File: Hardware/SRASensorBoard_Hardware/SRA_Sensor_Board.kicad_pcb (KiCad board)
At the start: 2 copper layers, 124.5 x 92.7 mm, 106 parts, among them J1 USB_A, Q1 BSS138, Q10 BSS138, Q11 BSS138, Q12 BSS138, Q13 BSS138, Q2 BSS138, Q3 BSS138, Q4 BSS138, Q5 BSS138, Q6 BSS138, Q7 Q_PMOS_GDS, Q8 Q_NMOS_GSD, Q9 BSS138, U1 OKI, U2 OKI, U3 FT230XS, U4 TM4C129E_Launchpad

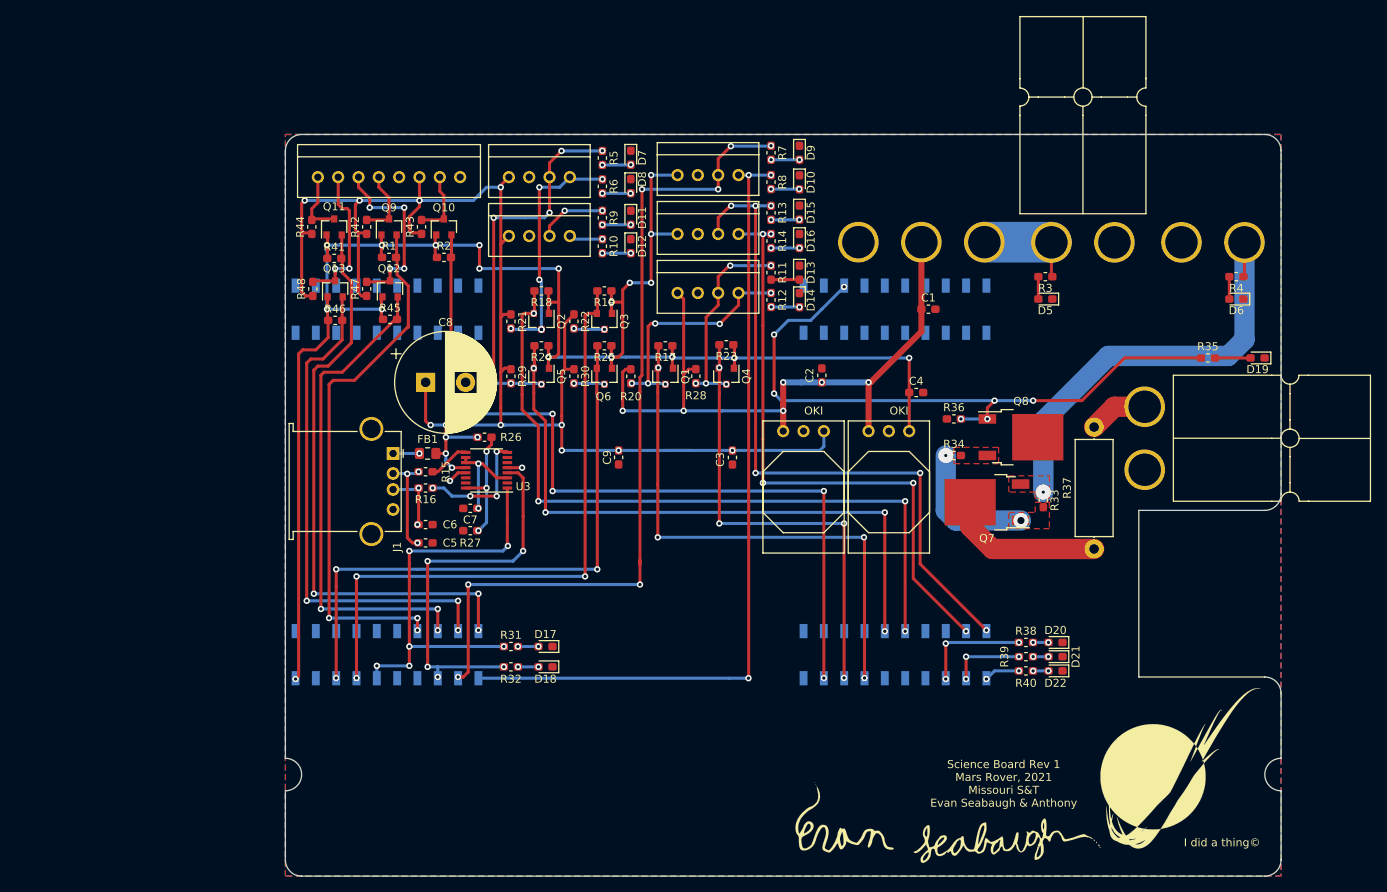
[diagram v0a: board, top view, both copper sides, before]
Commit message: Board Progress 6 (Post Review)
Finished moving vias off pads and labeling most things and added leds for spectrometer
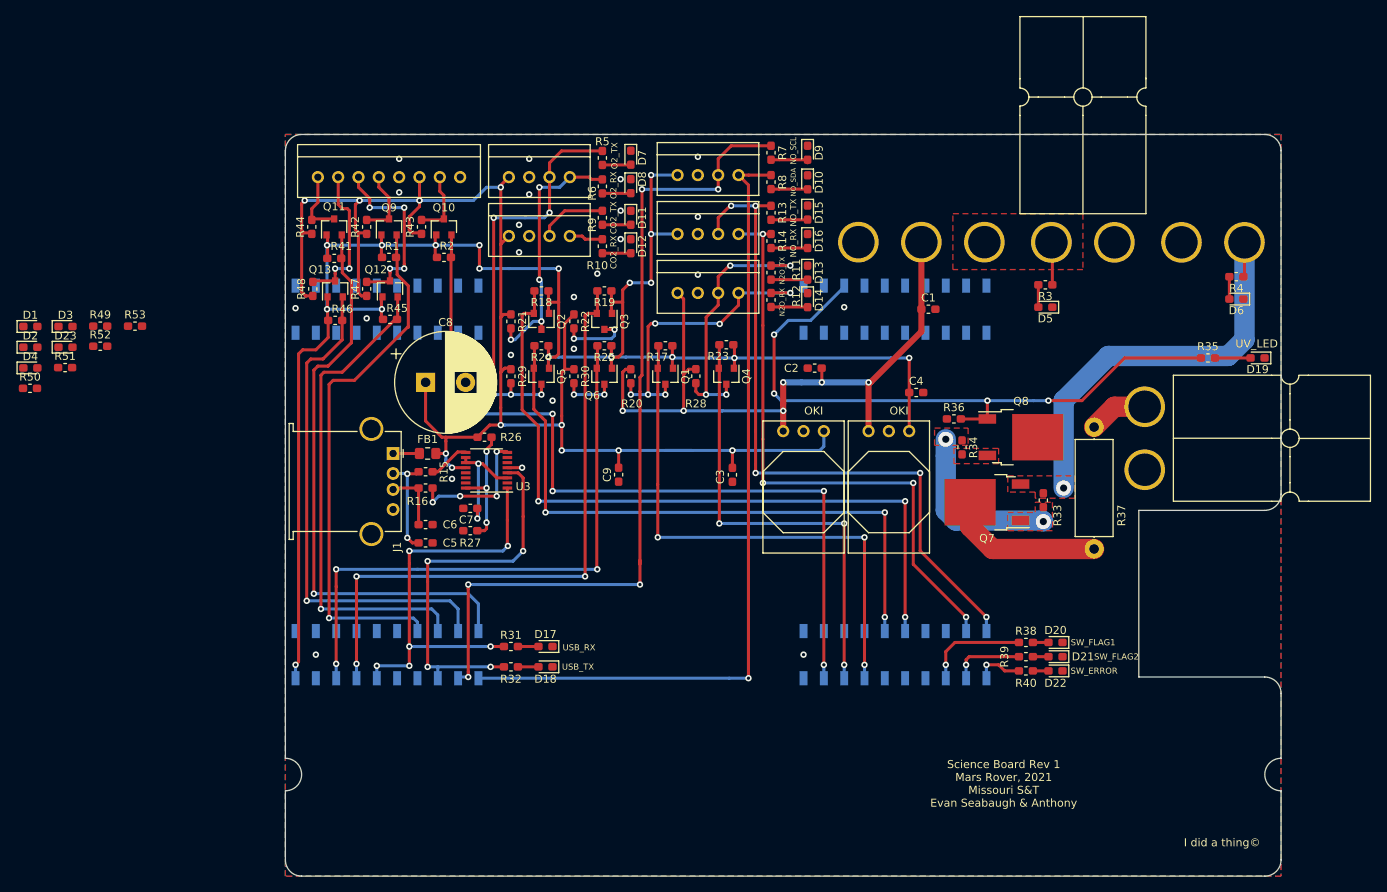
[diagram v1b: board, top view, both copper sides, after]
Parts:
- removed G***: LOGO, MRDT_Silkscreens:z_sig_Evan_Seabaugh_44mmx13.5mm
- removed G***: MRDT, MRDT_Silkscreens:0_MRDT_Logo_20mm
- added D1: LED, Diode_SMD:D_0603_1608Metric_Pad1.05x0.95mm_HandSolder, F.Cu at (59.6, 83.7)
- added D2: LED, Diode_SMD:D_0603_1608Metric_Pad1.05x0.95mm_HandSolder, F.Cu at (59.6, 86.3)
- added D23: LED, Diode_SMD:D_0603_1608Metric_Pad1.05x0.95mm_HandSolder, F.Cu at (64.0, 86.3)
- added D3: LED, Diode_SMD:D_0603_1608Metric_Pad1.05x0.95mm_HandSolder, F.Cu at (64.0, 83.7)
- added D4: LED, Diode_SMD:D_0603_1608Metric_Pad1.05x0.95mm_HandSolder, F.Cu at (59.6, 88.9)
- added R49: 330, Resistor_SMD:R_0603_1608Metric_Pad1.05x0.95mm_HandSolder, F.Cu at (68.3, 83.7)
- added R50: 330, Resistor_SMD:R_0603_1608Metric_Pad1.05x0.95mm_HandSolder, F.Cu at (59.5, 91.4)
- added R51: 330, Resistor_SMD:R_0603_1608Metric_Pad1.05x0.95mm_HandSolder, F.Cu at (63.9, 88.8)
- added R52: 330, Resistor_SMD:R_0603_1608Metric_Pad1.05x0.95mm_HandSolder, F.Cu at (68.3, 86.2)
- added R53: 330, Resistor_SMD:R_0603_1608Metric_Pad1.05x0.95mm_HandSolder, F.Cu at (72.6, 83.7)
- moved C3 2.16 mm to (147.3, 102.2)
- moved C9 2.16 mm to (133.1, 102.2)
- moved R34 1.44 mm to (176.0, 98.8), turned to 270 degrees
- moved C2 1.27 mm to (157.6, 88.9), turned to 180 degrees
- moved D5 1.02 mm to (186.4, 81.3)
- moved R3 1.02 mm to (186.4, 78.5)
- moved D10 1.02 mm to (156.7, 65.7)
- moved D13 1.02 mm to (156.7, 77.0)
- moved D14 1.02 mm to (156.7, 80.4)
- moved D15 1.02 mm to (156.7, 69.5)
- moved D16 1.02 mm to (156.7, 73.0)
- moved D9 1.02 mm to (156.7, 62.0)
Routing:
- net N2O_RX: track 29.9 -> 38.5 mm
- net N2O_TX: track 25.3 -> 33.7 mm, vias 5 -> 4
- net +12VA: track 12.7 -> 5.55 mm
- net Net-(Q7-Pad1): track 16.8 -> 21.7 mm
- net C02_RX: track 4.03 -> 8.74 mm
- net O2_TX: track 47.6 -> 51.5 mm, vias 7 -> 5
- net O2_RX: track 30.4 -> 33.0 mm, vias 6 -> 4
- net Net-(C7-Pad1): track 12.2 -> 14.8 mm
- net C02_TX: track 4.03 -> 6.51 mm
- net GND: track 4.44 -> 2.05 mm, vias 2 -> 24
- net +12V: track 86.5 -> 88.3 mm
- net Net-(R16-Pad1): track 15.4 -> 17.1 mm
- net SW_ERROR: track 4.48 -> 6.06 mm, vias 2 -> 1
- net +24V: track 54.8 -> 53.2 mm
- net Net-(D9-Pad2): track 3.60 -> 4.63 mm, vias 2 -> 0
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- added copper zone on F.Cu, net +12VA
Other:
- board text added: "+"
- board text added: "-"
- board text added: "BUCK_12V_IN"
- board text added: "BUCK_24V_IN"
- board text added: "CLP"
- board text added: "CO2_RX"
- board text added: "CO2_SL"
- board text added: "CO2_TX"
- board text added: "D_IN"
- board text added: "D_OUT"
- board text added: "EOS"
- board text added: "HeLp"
- board text added: "N2O_RX"
- board text added: "N2O_SL"
- board text added: "N2O_TX"
- board text added: "NO2_SL"
- board text added: "NO_RX"
- board text added: "NO_SCL"
- board text added: "NO_SDA"
- board text added: "NO_SL"
- board text added: "NO_TX"
- board text added: "O2_RX"
- board text added: "O2_SL"
- board text added: "O2_TX"
- board text added: "POWER_IN"
- board text added: "RX"
- board text added: "SCL"
- board text added: "SDA"
- board text added: "SP"
- board text added: "SW_ERROR"
- board text added: "SW_FLAG1"
- board text added: "SW_FLAG2"
- board text added: "TP"
- board text added: "TX"
- board text added: "USB_RX"
- board text added: "USB_TX"
- board text added: "UV_LED"
- board text added: "VA"
- board text added: "VD"
- board text added: "_"

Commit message: Board Progress 7 (final rev 1)
Final edits for REV 1
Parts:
- added G***: LOGO, MRDT_Silkscreens:0_MRDT_Logo_20mm, F.Cu at (203.3, 138.4)
- added G***: LOGO, MRDT_Silkscreens:z_sig_Evan_Seabaugh_44mmx13.5mm, F.Cu at (175.5, 147.1)
- C8: footprint Capacitor_THT:CP_Radial_D12.5mm_P5.00mm -> Capacitor_THT:CP_Radial_D5.0mm_P2.50mm
- moved D2 77.8 mm to (128.3, 122.8), turned to 180 degrees
- moved D1 75.8 mm to (128.3, 115.7), turned to 180 degrees
- moved D4 75.1 mm to (128.3, 119.3), turned to 180 degrees
- moved D3 74.4 mm to (128.3, 121.0), turned to 180 degrees
- moved R50 71.7 mm to (124.0, 122.8)
- moved D23 71.5 mm to (128.3, 117.5), turned to 180 degrees
- moved R51 68.1 mm to (124.0, 121.0)
- moved R52 64.7 mm to (124.0, 119.3)
- moved R49 64.2 mm to (124.0, 115.7)
- moved R53 61.4 mm to (124.0, 117.5)
- moved C8 2.67 mm to (109.0, 93.3), turned to 90 degrees
- moved D17 0.76 mm to (124.0, 124.5)
- moved R31 0.76 mm to (119.6, 124.5)
- moved C5 0.64 mm to (109.0, 110.1)
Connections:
- J1 pad 5: Net-(J1-Pad5) -> GND
- R49 pad 1: Clock_Pulse -> TIVA_EOS
- R50 pad 1: Video -> TIVA_Video
- R51 pad 1: Start_Pulse -> TIVA_Clock_Pulse
- R52 pad 1: Trigger_Pulse -> TIVA_Trigger_Pulse
- R53 pad 1: EOS -> TIVA_Start_Pulse
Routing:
- net TIVA_Clock_Pulse: track 61.4 -> 78.4 mm, vias 1 -> 4
- net TIVA_Video: track 66.8 -> 83.3 mm, vias 1 -> 3
- net TIVA_Trigger_Pulse: track 62.9 -> 77.1 mm, vias 1 -> 4
- net TIVA_EOS: track 102.2 -> 114.3 mm
- net TIVA_Start_Pulse: track 72.7 -> 84.2 mm, vias 1 -> 4
- net +5V: track 190.3 -> 187.6 mm
- net Net-(D4-Pad2): track 0.00 -> 2.57 mm
- net Net-(D3-Pad2): track 0.00 -> 2.57 mm
- net Net-(D23-Pad2): track 0.00 -> 2.57 mm
- net Net-(D2-Pad2): track 0.00 -> 2.57 mm
- net Net-(D1-Pad2): track 0.00 -> 2.57 mm
- net TIVA_CO2_RX: track 74.4 -> 75.4 mm
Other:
- board text added: "CLOCK_PULSE"
- board text added: "START_PULSE"
- board text added: "TRIGGER_PULSE"
- board text added: "VIDEO"

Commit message: Fixed some library issues
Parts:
- C1, C2, C3, C4, C5, C6, C7, C9: footprint Capacitor_SMD:C_0603_1608Metric_Pad1.05x0.95mm_HandSolder -> Capacitor_SMD:C_0603_1608Metric_Pad1.08x0.95mm_HandSolder
- FB1: footprint Resistor_SMD:R_0805_2012Metric_Pad1.15x1.40mm_HandSolder -> Resistor_SMD:R_0805_2012Metric_Pad1.20x1.40mm_HandSolder
- R1, R13, R14, R15, R16, R17, R18, R19, R2, R20, R21, R22, R23, R24, R25, R26, R27, R28, R29, R30, R33, R34, R36, R41, R42, R43, R44, R45, R46, R47, R48, R7, R8: footprint Resistor_SMD:R_0603_1608Metric_Pad1.05x0.95mm_HandSolder -> Resistor_SMD:R_0603_1608Metric_Pad0.98x0.95mm_HandSolder
- R10, R31, R32, R35, R38, R39, R40, R49, R5, R50, R51, R52, R53, R6, R9: value 330 -> 480; footprint Resistor_SMD:R_0603_1608Metric_Pad1.05x0.95mm_HandSolder -> Resistor_SMD:R_0603_1608Metric_Pad0.98x0.95mm_HandSolder
- R11, R12: value 330 -> 1K; footprint Resistor_SMD:R_0603_1608Metric_Pad1.05x0.95mm_HandSolder -> Resistor_SMD:R_0603_1608Metric_Pad0.98x0.95mm_HandSolder
- R3: value 1000 -> 1K; footprint Resistor_SMD:R_0603_1608Metric_Pad1.05x0.95mm_HandSolder -> Resistor_SMD:R_0603_1608Metric_Pad0.98x0.95mm_HandSolder
- R4: value 2500 -> 2.5K; footprint Resistor_SMD:R_0603_1608Metric_Pad1.05x0.95mm_HandSolder -> Resistor_SMD:R_0603_1608Metric_Pad0.98x0.95mm_HandSolder
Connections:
- U4 pad +3V3': (no net) -> +3V3
- U4 pad +5V': (no net) -> Net-(U4-Pad+5V')
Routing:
- net +24V: track 53.2 -> 4.35 mm, vias 1 -> 5
- net +3V3: track 228.2 -> 271.1 mm, vias 18 -> 20
- net Net-(Q7-Pad1): track 21.7 -> 0.00 mm, vias 2 -> 10
- net GND: vias 24 -> 69
- added copper zone on B.Cu, net +12VA
- added copper zone on B.Cu, net +24V
- added copper zone on B.Cu, net Net-(Q7-Pad1)

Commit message: Fixed Gerbs and step file
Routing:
- net +24V: track 4.35 -> 8.64 mm
- net GND: vias 69 -> 78
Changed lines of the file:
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@@
     (thickness 1.6)
     (drawings 93)
-    (tracks 958)
+    (tracks 968)
     (zones 0)
     (modules 116)
@@
   )
   (setup
-    (last_trace_width 0.25)
+    (last_trace_width 1.27)
     (user_trace_width 0.254)
     (user_trace_width 0.254)
@@
   (via (at 157.988 100.076) (size 0.8) (drill 0.4) (layers F.Cu B.Cu) (net 1))
   (via (at 153.924 100.076) (size 0.8) (drill 0.4) (layers F.Cu B.Cu) (net 1))
+  (via (at 213.614 84.582) (size 0.8) (drill 0.4) (layers F.Cu B.Cu) (net 1))
+  (via (at 213.614 81.534) (size 0.8) (drill 0.4) (layers F.Cu B.Cu) (net 1))
+  (via (at 213.614 78.486) (size 0.8) (drill 0.4) (layers F.Cu B.Cu) (net 1))
+  (via (at 213.614 76.2) (size 0.8) (drill 0.4) (layers F.Cu B.Cu) (net 1))
+  (via (at 212.598 66.802) (size 0.8) (drill 0.4) (layers F.Cu B.Cu) (net 1))
+  (via (at 207.518 66.802) (size 0.8) (drill 0.4) (layers F.Cu B.Cu) (net 1))
+  (via (at 201.676 66.802) (size 0.8) (drill 0.4) (layers F.Cu B.Cu) (net 1))
+  (via (at 195.834 66.802) (size 0.8) (drill 0.4) (layers F.Cu B.Cu) (net 1))
+  (via (at 191.77 66.802) (size 0.8) (drill 0.4) (layers F.Cu B.Cu) (net 1))
   (segment (start 170.942 73.152) (end 170.942 84.328) (width 0.762) (layer F.Cu) (net 2) (status 10))
   (segment (start 170.942 84.328) (end 164.592 90.678) (width 0.762) (layer F.Cu) (net 2))
@@
   (via (at 187.96 104.394) (size 0.8) (drill 0.4) (layers F.Cu B.Cu) (net 9))
   (via (at 188.976 103.632) (size 0.8) (drill 0.4) (layers F.Cu B.Cu) (net 9))
+  (segment (start 211.328 73.1774) (end 211.328 77.47) (width 1.27) (layer B.Cu) (net 9))
   (segment (start 185.561 78.486) (end 185.561 81.28) (width 0.381) (layer F.Cu) (net 10) (status 30))
   (segment (start 209.437 77.47) (end 209.437 80.264) (width 0.381) (layer F.Cu) (net 11) (status 30))
@@
     (polygon
       (pts
-        (xy 208.026 69.85) (xy 207.899 85.598) (xy 187.0075 85.598) (xy 186.944 105.156) (xy 191.008 105.156)
-        (xy 191.008 89.662) (xy 195.961 89.662) (xy 207.264 89.662) (xy 214.63 89.662) (xy 214.63 69.85)
+        (xy 208.5975 69.85) (xy 208.4705 85.598) (xy 187.22975 85.598) (xy 187.16625 105.156) (xy 190.754 105.156)
+        (xy 190.754 89.154) (xy 212.344 89.154) (xy 212.344 69.85)
       )
     )
@@
     (polygon
       (pts
-        (xy 187.452 109.728) (xy 172.466 109.728) (xy 172.466 96.266) (xy 176.53 96.266) (xy 176.53 105.664)
-        (xy 187.452 105.664)
+        (xy 187.452 110.236) (xy 172.466 110.236) (xy 172.466 96.266) (xy 176.022 96.266) (xy 176.022 106.68)
+        (xy 187.452 106.68)
       )
     )

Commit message: Finished BOM
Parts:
- D1, D10, D11, D12, D13, D14, D15, D16, D17, D18, D2, D20, D21, D23, D3, D4, D7, D8, D9: value LED -> Blue
- D19: value LED -> Yellow
- D22: value LED -> Red
- D5, D6: value LED -> Green
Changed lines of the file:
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@@
   )
   (setup
-    (last_trace_width 1.27)
+    (last_trace_width 0.25)
     (user_trace_width 0.254)
     (user_trace_width 0.254)
@@
       (effects (font (size 1 1) (thickness 0.15)))
     )
-    (fp_text value LED (at 0 1.43) (layer F.Fab)
+    (fp_text value Blue (at 0 1.43) (layer F.Fab)
       (effects (font (size 1 1) (thickness 0.15)))
     )
@@
       (effects (font (size 1 1) (thickness 0.15)))
     )
-    (fp_text value LED (at 0 1.43) (layer F.Fab)
+    (fp_text value Blue (at 0 1.43) (layer F.Fab)
       (effects (font (size 1 1) (thickness 0.15)))
     )
@@
       (effects (font (size 1 1) (thickness 0.15)))
     )
-    (fp_text value LED (at 0 1.43) (layer F.Fab)
+    (fp_text value Blue (at 0 1.43) (layer F.Fab)
       (effects (font (size 1 1) (thickness 0.15)))
     )
@@
       (effects (font (size 1 1) (thickness 0.15)))
     )
-    (fp_text value LED (at 0 1.43) (layer F.Fab)
+    (fp_text value Blue (at 0 1.43) (layer F.Fab)
       (effects (font (size 1 1) (thickness 0.15)))
     )
@@
       (effects (font (size 1 1) (thickness 0.15)))
     )
-    (fp_text value LED (at 0 1.43) (layer F.Fab)
+    (fp_text value Blue (at 0 1.43) (layer F.Fab)
       (effects (font (size 1 1) (thickness 0.15)))
     )
@@
       (effects (font (size 1 1) (thickness 0.15)))
     )
-    (fp_text value LED (at 0 1.43 90) (layer F.Fab)
+    (fp_text value Blue (at 0 1.43 90) (layer F.Fab)
       (effects (font (size 1 1) (thickness 0.15)))
     )
@@
       (effects (font (size 1 1) (thickness 0.15)))
     )
-    (fp_text value LED (at 0 1.43) (layer F.Fab)
+    (fp_text value Red (at 0 1.43) (layer F.Fab)
       (effects (font (size 1 1) (thickness 0.15)))
     )
@@
       (effects (font (size 1 1) (thickness 0.15)))
     )
-    (fp_text value LED (at 0 1.43) (layer F.Fab)
+    (fp_text value Blue (at 0 1.43) (layer F.Fab)
       (effects (font (size 1 1) (thickness 0.15)))
     )
@@
       (effects (font (size 1 1) (thickness 0.15)))
     )
-    (fp_text value LED (at 0 1.43) (layer F.Fab)
+    (fp_text value Blue (at 0 1.43) (layer F.Fab)
       (effects (font (size 1 1) (thickness 0.15)))
     )
@@
       (effects (font (size 1 1) (thickness 0.15)))
     )
-    (fp_text value LED (at 0 1.43) (layer F.Fab)
+    (fp_text value Yellow (at 0 1.43) (layer F.Fab)
       (effects (font (size 1 1) (thickness 0.15)))
     )
@@
       (effects (font (size 1 1) (thickness 0.15)))
     )
-    (fp_text value LED (at 0 1.43) (layer F.Fab)
+    (fp_text value Blue (at 0 1.43) (layer F.Fab)
       (effects (font (size 1 1) (thickness 0.15)))
     )
@@
       (effects (font (size 1 1) (thickness 0.15)))
     )
-    (fp_text value LED (at 0 1.43) (layer F.Fab)
+    (fp_text value Blue (at 0 1.43) (layer F.Fab)
       (effects (font (size 1 1) (thickness 0.15)))
     )
@@
       (effects (font (size 1 1) (thickness 0.15)))
     )
-    (fp_text value LED (at 0 1.43 90) (layer F.Fab)
+    (fp_text value Blue (at 0 1.43 90) (layer F.Fab)
       (effects (font (size 1 1) (thickness 0.15)))
     )
@@
       (effects (font (size 1 1) (thickness 0.15)))
     )
-    (fp_text value LED (at 0 1.43 90) (layer F.Fab)
+    (fp_text value Blue (at 0 1.43 90) (layer F.Fab)
       (effects (font (size 1 1) (thickness 0.15)))
     )
@@
       (effects (font (size 1 1) (thickness 0.15)))
     )
-    (fp_text value LED (at 0 1.43 90) (layer F.Fab)
+    (fp_text value Blue (at 0 1.43 90) (layer F.Fab)
       (effects (font (size 1 1) (thickness 0.15)))
     )
@@
       (effects (font (size 1 1) (thickness 0.15)))
     )
-    (fp_text value LED (at 0 1.43 90) (layer F.Fab)
+    (fp_text value Blue (at 0 1.43 90) (layer F.Fab)
       (effects (font (size 1 1) (thickness 0.15)))
     )
@@
       (effects (font (size 1 1) (thickness 0.15)))
     )
-    (fp_text value LED (at 0 1.43 90) (layer F.Fab)
+    (fp_text value Blue (at 0 1.43 90) (layer F.Fab)
       (effects (font (size 1 1) (thickness 0.15)))
     )
@@
       (effects (font (size 1 1) (thickness 0.15)))
     )
-    (fp_text value LED (at 0 1.43 90) (layer F.Fab)
+    (fp_text value Blue (at 0 1.43 90) (layer F.Fab)
       (effects (font (size 1 1) (thickness 0.15)))
     )
@@
       (effects (font (size 1 1) (thickness 0.15)))
     )
-    (fp_text value LED (at 0 1.43 90) (layer F.Fab)
+    (fp_text value Blue (at 0 1.43 90) (layer F.Fab)
       (effects (font (size 1 1) (thickness 0.15)))
     )
@@
       (effects (font (size 1 1) (thickness 0.15)))
     )
-    (fp_text value LED (at 0 1.43 90) (layer F.Fab)
+    (fp_text value Blue (at 0 1.43 90) (layer F.Fab)
       (effects (font (size 1 1) (thickness 0.15)))
     )
@@
       (effects (font (size 1 1) (thickness 0.15)))
     )
-    (fp_text value LED (at 0 1.43 90) (layer F.Fab)
+    (fp_text value Blue (at 0 1.43 90) (layer F.Fab)
       (effects (font (size 1 1) (thickness 0.15)))
     )
@@
       (effects (font (size 1 1) (thickness 0.15)))
     )
-    (fp_text value LED (at 0 1.43) (layer F.Fab)
+    (fp_text value Green (at 0 1.43) (layer F.Fab)
       (effects (font (size 1 1) (thickness 0.15)))
     )
@@
       (effects (font (size 1 1) (thickness 0.15)))
     )
-    (fp_text value LED (at 0 1.43) (layer F.Fab)
+    (fp_text value Green (at 0 1.43) (layer F.Fab)
       (effects (font (size 1 1) (thickness 0.15)))
     )
